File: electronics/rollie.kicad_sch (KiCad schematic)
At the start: 13 parts, among them J1 Jack-DC, J2 Vcc, J3 Probe, J4 Relay In, J5 Vcc, J6 Serial, J7 Servo PWM, J8 Probe, K1 DIPxx-1Cxx-51x, SW1 SW_Push

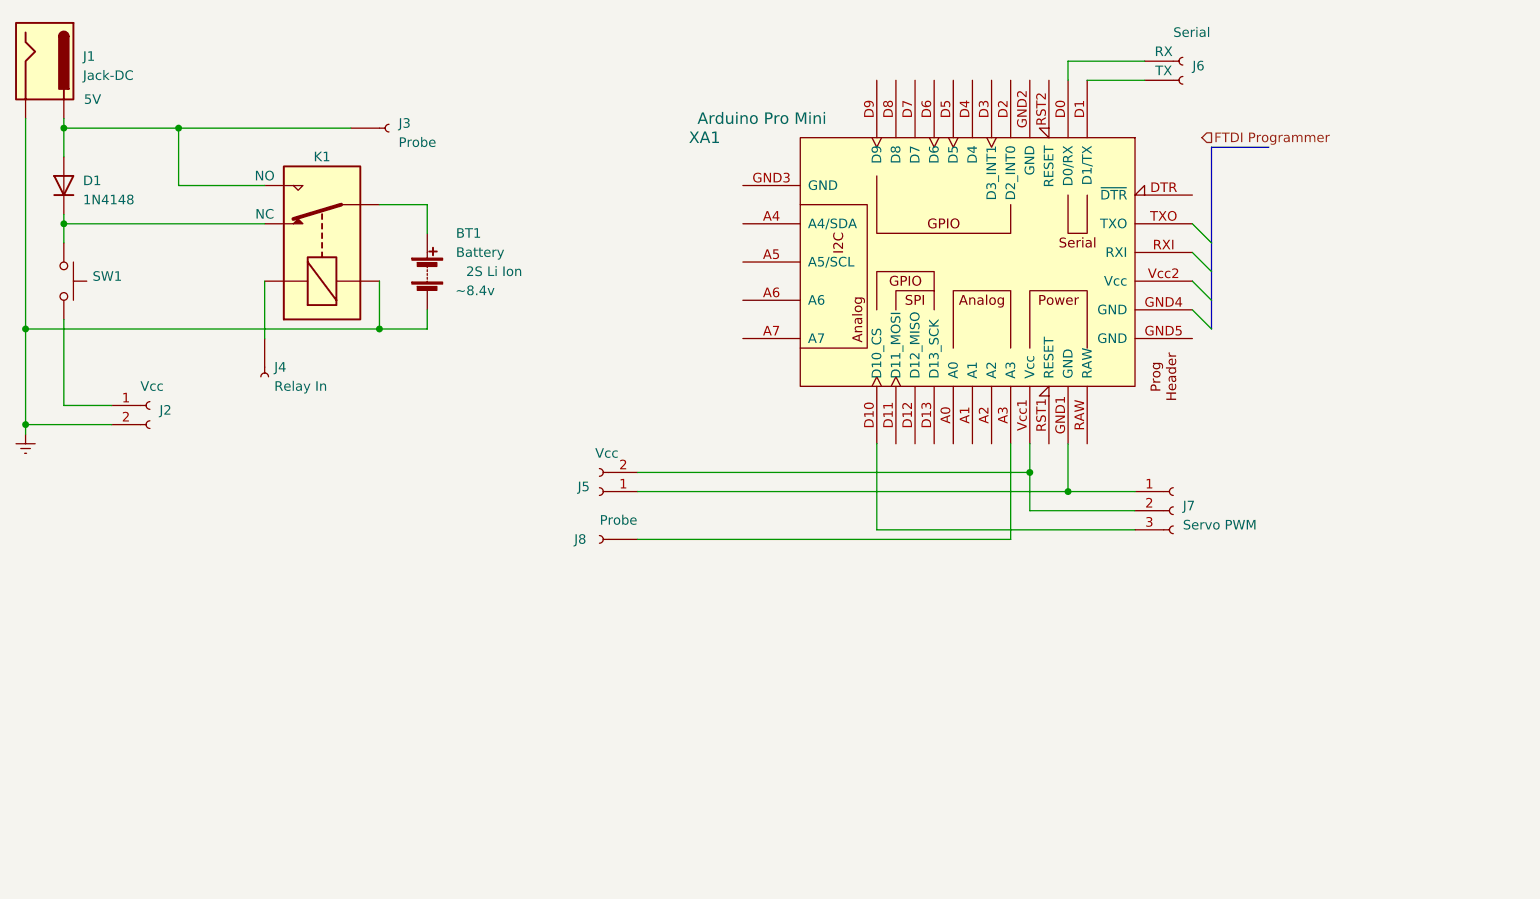
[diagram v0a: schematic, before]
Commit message: Adding motors, L298N, Probe
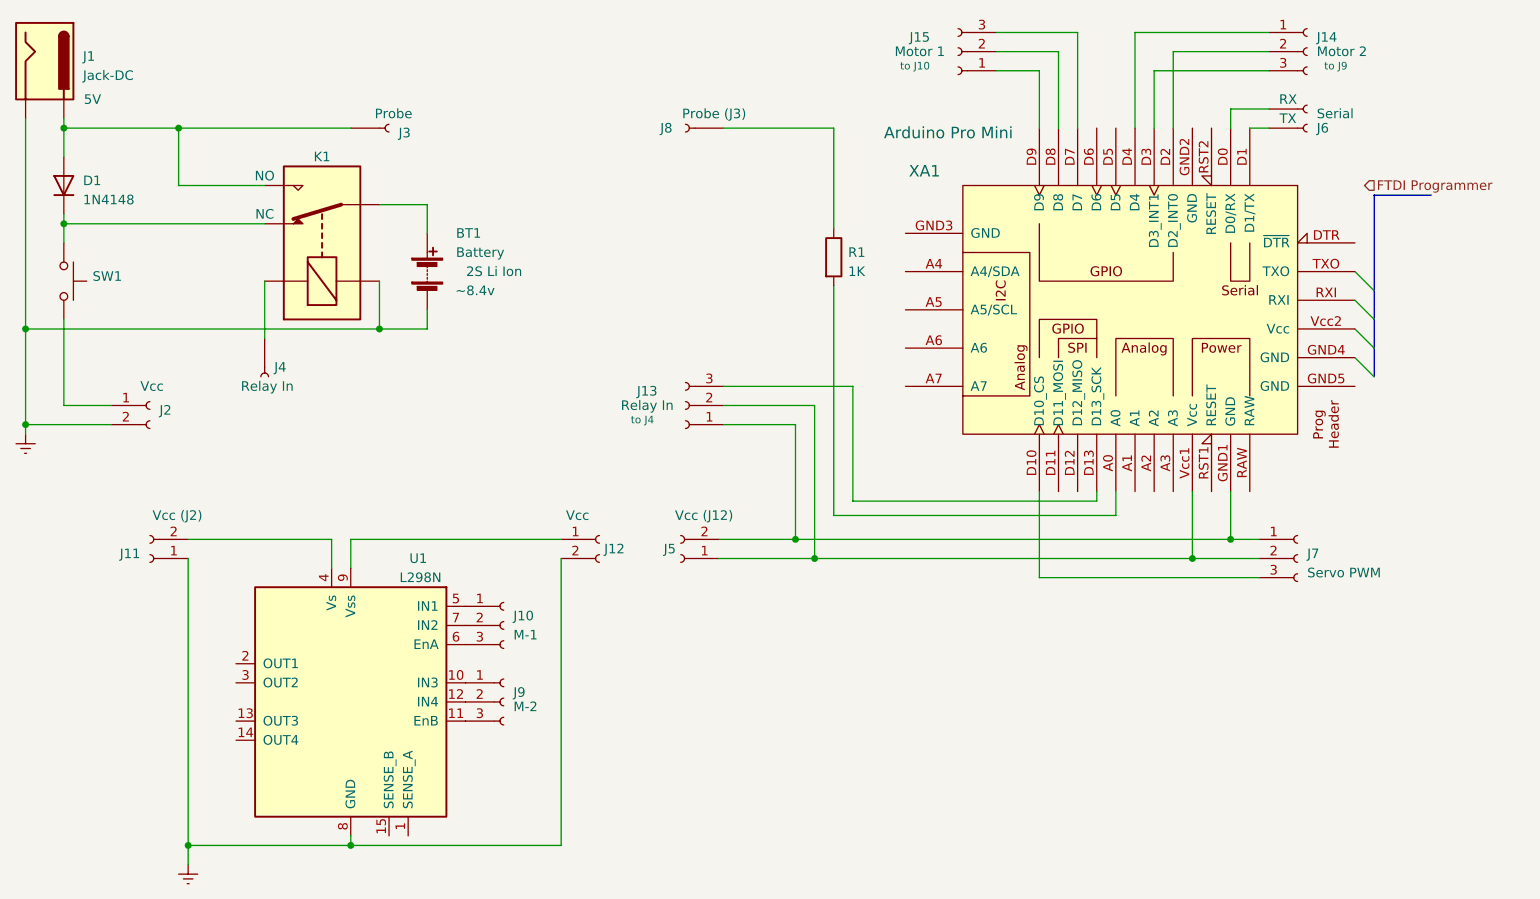
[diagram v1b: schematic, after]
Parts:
- added J10: M-1, symbol Connector:Conn_01x03_Socket
- added J11: Vcc (J2), symbol Connector:Conn_01x02_Socket
- added J12: Vcc, symbol Connector:Conn_01x02_Socket
- added J13: Relay In, symbol Connector:Conn_01x03_Socket
- added J14: Motor 2, symbol Connector:Conn_01x03_Socket
- added J15: Motor 1, symbol Connector:Conn_01x03_Socket
- added J9: M-2, symbol Connector:Conn_01x03_Socket
- added R1: 1K, symbol Device:R
- added U1: L298N, Package_TO_SOT_THT:TO-220-15_P2.54x2.54mm_StaggerOdd_Lead4.58mm_Vertical, symbol Driver_Motor:L298N
- J5: value Vcc -> Vcc (J12)
- J8: value Probe -> Probe (J3)
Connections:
- net Earth: now also J11.1 (Pin_1), J12.2 (Pin_2), U1.8 (GND)
- net at J8.1 (Pin_1): now also R1.1; no longer XA1.A3
- net at XA1.A0: now also R1.2
- net at XA1.D13 (D13_SCK): now also J13.3 (Pin_3)
- net at XA1.D2 (D2_INT0): now also J14.2 (Pin_2)
- net at XA1.D3 (D3_INT1): now also J14.3 (Pin_3)
- net at XA1.D4: now also J14.1 (Pin_1)
- net at XA1.D7: now also J15.3 (Pin_3)
- net at XA1.D8: now also J15.2 (Pin_2)
- net at XA1.D9: now also J15.1 (Pin_1)
- net at J7.1 (Pin_1), XA1.GND1 (GND): now also J5.2 (Pin_2), J13.1 (Pin_1); no longer J5.1 (Pin_1)
- net at J7.2 (Pin_2), XA1.Vcc1 (Vcc): now also J5.1 (Pin_1), J13.2 (Pin_2); no longer J5.2 (Pin_2)
- new net: J9.1 (Pin_1), U1.10 (IN3)
- new net: J9.3 (Pin_3), U1.11 (EnB)
- new net: J9.2 (Pin_2), U1.12 (IN4)
- new net: J11.2 (Pin_2), U1.4 (Vs)
- new net: J10.1 (Pin_1), U1.5 (IN1)
- new net: J10.3 (Pin_3), U1.6 (EnA)
- new net: J10.2 (Pin_2), U1.7 (IN2)
- new net: J12.1 (Pin_1), U1.9 (Vss)
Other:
- moved on the sheet: J5, J6, J7, J8, XA1

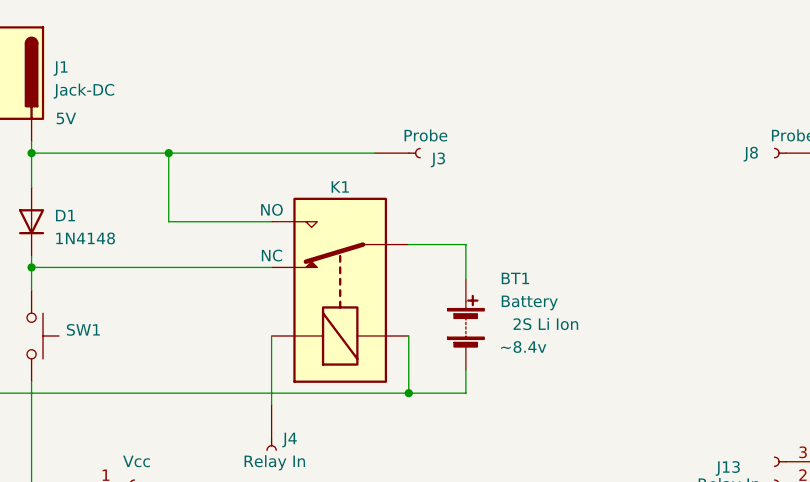
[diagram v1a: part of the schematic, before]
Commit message: schema with relay
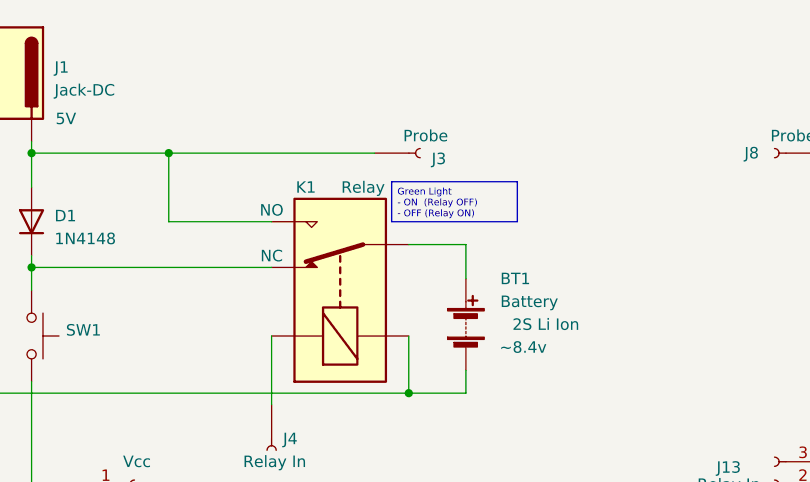
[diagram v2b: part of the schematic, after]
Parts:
- K1: Field6 (none) -> Relay
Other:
- company: (none) -> Ben
- title: (none) -> Rollie Robot Schematics
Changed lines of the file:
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@@
 (kicad_sch (version 20230121) (generator eeschema)
   (paper "A4")
+  (title_block
+    (title "Rollie Robot Schematics")
+    (date "2023-03-26")
+    (rev "1.0")
+    (company "Ben")
+    (comment 1 "                   overall schematics and circuitry")
+    (comment 3 "                   Rollie Schematics")
+  )
   (junction (at 30.48 29.21) (diameter 0) (color 0 0 0 0)
   )
@@
   (wire (pts (xy 170.18 80.645) (xy 132.715 80.645))
     (stroke (width 0) (type default))
+  )
+  (text_box "Green Light\n- ON  (Relay OFF)\n- OFF (Relay ON)"
+    (at 70.485 32.385 0) (size 13.97 4.445)
+    (stroke (width 0.1) (type default) (color 132 0 0 1))
+    (fill (type color) (color 255 251 183 1))
+    (effects (font (size 0.75 0.75) (color 132 0 0 1)) (justify left top))
   )
   (hierarchical_label "FTDI Programmer" (shape input) (at 203.2 36.83 0) (fields_autoplaced)
@@
   (symbol (lib_id "Relay:DIPxx-1Cxx-51x") (at 64.77 44.45 90) (unit 1)
     (in_bom yes) (on_board yes) (dnp no)
-    (property "Reference" "K1" (at 64.77 33.02 90)
+    (property "Reference" "K1" (at 60.96 33.02 90)
       (effects (font (size 1.27 1.27)))
     )
@@
       (effects (font (size 1.27 1.27)))
     )
+    (property "Field6" "Relay" (at 67.31 33.02 90)
+      (effects (font (size 1.27 1.27)))
+    )
